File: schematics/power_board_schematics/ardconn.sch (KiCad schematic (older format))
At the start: 1 part, among them J7 CONN_01X16

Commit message: Change Power board Arduino connector
Also, the 15v power regulator no longer shorts its NC pins to ground
(this isn't changed in this commit, it was changed before these
schematics were added to github).
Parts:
- J7: footprint Socket_Strips:Socket_Strip_Straight_2x08_Pitch2.00mm -> Pin_Headers:Pin_Header_Straight_2x08_Pitch2.54mm
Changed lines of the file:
@@
 F 0 "J7" H 7300 4600 50  0000 C CNN
 F 1 "CONN_01X16" V 7400 3750 50  0000 C CNN
-F 2 "Socket_Strips:Socket_Strip_Straight_2x08_Pitch2.00mm" H 7300 3750 50  0001 C CNN
+F 2 "Pin_Headers:Pin_Header_Straight_2x08_Pitch2.54mm" H 7300 3750 50  0001 C CNN
 F 3 "" H 7300 3750 50  0001 C CNN
 	1    7300 3750

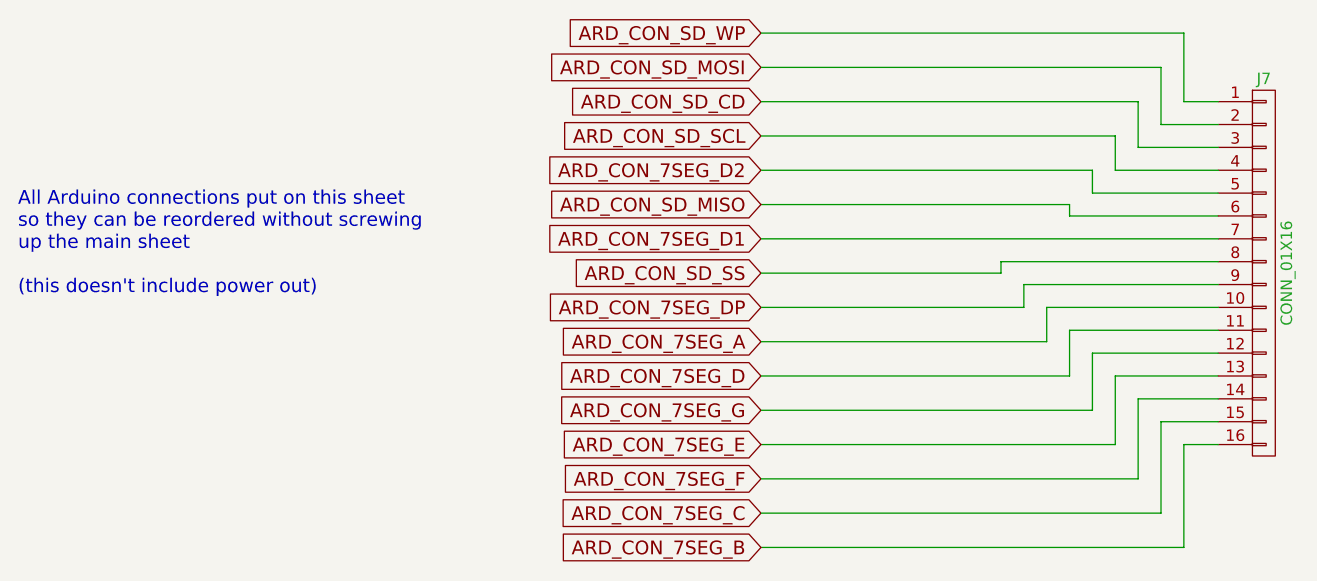
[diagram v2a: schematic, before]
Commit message: Actually make it a 2.54mm pitch connector
whoops, I had a 2mm pitch one, now it's fixed and is proper. DRC passes
with flying colours.
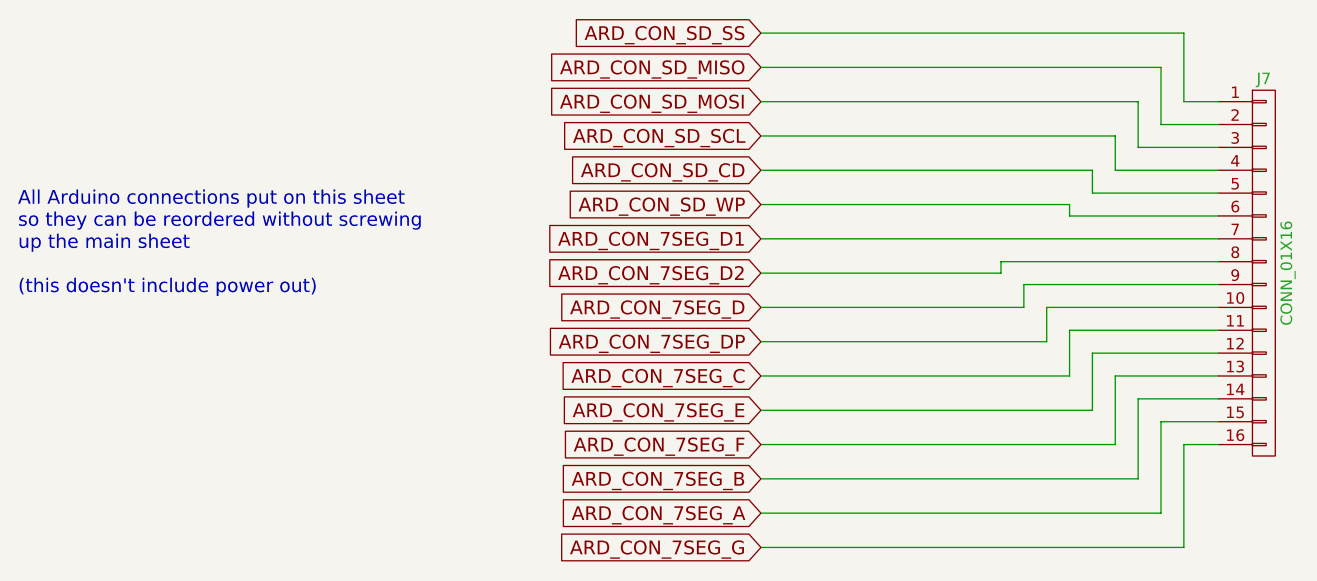
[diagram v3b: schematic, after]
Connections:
- net ARD_CON_7SEG_A: now also J7.15 (P15); no longer J7.10 (P10)
- net ARD_CON_7SEG_B: now also J7.14 (P14); no longer J7.16 (P16)
- net ARD_CON_7SEG_C: now also J7.11 (P11); no longer J7.15 (P15)
- net ARD_CON_7SEG_D: now also J7.9 (P9); no longer J7.11 (P11)
- net ARD_CON_7SEG_D2: now also J7.8 (P8); no longer J7.5 (P5)
- net ARD_CON_7SEG_DP: now also J7.10 (P10); no longer J7.9 (P9)
- net ARD_CON_7SEG_E: now also J7.12 (P12); no longer J7.13 (P13)
- net ARD_CON_7SEG_F: now also J7.13 (P13); no longer J7.14 (P14)
- net ARD_CON_7SEG_G: now also J7.16 (P16); no longer J7.12 (P12)
- net ARD_CON_SD_CD: now also J7.5 (P5); no longer J7.3 (P3)
- net ARD_CON_SD_MISO: now also J7.2 (P2); no longer J7.6 (P6)
- net ARD_CON_SD_MOSI: now also J7.3 (P3); no longer J7.2 (P2)
- net ARD_CON_SD_SS: now also J7.1 (P1); no longer J7.8 (P8)
- net ARD_CON_SD_WP: now also J7.6 (P6); no longer J7.1 (P1)
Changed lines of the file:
@@
 $Descr A4 11693 8268
 encoding utf-8
-Sheet 5 2
+Sheet 2 2
 Title "RLCS power board"
 Date "2017-09-24"
@@
 Comment4 ""
 $EndDescr
-Text GLabel 5100 2850 0    60   Input ~ 0
+Text GLabel 5100 3000 0    60   Input ~ 0
 ARD_CON_SD_MOSI
 Text GLabel 5100 3150 0    60   Input ~ 0
 ARD_CON_SD_SCL
-Text GLabel 5100 3750 0    60   Input ~ 0
+Text GLabel 5100 2700 0    60   Input ~ 0
 ARD_CON_SD_SS
-Text GLabel 5100 2700 0    60   Input ~ 0
+Text GLabel 5100 3450 0    60   Input ~ 0
 ARD_CON_SD_WP
-Text GLabel 5100 3000 0    60   Input ~ 0
+Text GLabel 5100 3300 0    60   Input ~ 0
 ARD_CON_SD_CD
+Text GLabel 5100 4800 0    60   Input ~ 0
+ARD_CON_7SEG_A
+Text GLabel 5100 4650 0    60   Input ~ 0
+ARD_CON_7SEG_B
+Text GLabel 5100 4200 0    60   Input ~ 0
+ARD_CON_7SEG_C
+Text GLabel 5100 3900 0    60   Input ~ 0
+ARD_CON_7SEG_D
+Text GLabel 5100 4350 0    60   Input ~ 0
+ARD_CON_7SEG_E
+Text GLabel 5100 4500 0    60   Input ~ 0
+ARD_CON_7SEG_F
+Text GLabel 5100 4950 0    60   Input ~ 0
+ARD_CON_7SEG_G
 Text GLabel 5100 4050 0    60   Input ~ 0
-ARD_CON_7SEG_A
-Text GLabel 5100 4950 0    60   Input ~ 0
-ARD_CON_7SEG_B
-Text GLabel 5100 4800 0    60   Input ~ 0
-ARD_CON_7SEG_C
-Text GLabel 5100 4200 0    60   Input ~ 0
-ARD_CON_7SEG_D
-Text GLabel 5100 4500 0    60   Input ~ 0
-ARD_CON_7SEG_E
-Text GLabel 5100 4650 0    60   Input ~ 0
-ARD_CON_7SEG_F
-Text GLabel 5100 4350 0    60   Input ~ 0
-ARD_CON_7SEG_G
-Text GLabel 5100 3900 0    60   Input ~ 0
 ARD_CON_7SEG_DP
 Text GLabel 5100 3600 0    60   Input ~ 0
 ARD_CON_7SEG_D1
-Text GLabel 5100 3300 0    60   Input ~ 0
+Text GLabel 5100 3750 0    60   Input ~ 0
 ARD_CON_7SEG_D2
-Text GLabel 5100 3450 0    60   Input ~ 0
+Text GLabel 5100 2850 0    60   Input ~ 0
 ARD_CON_SD_MISO
 Text Notes 1850 3850 0    60   ~ 0
